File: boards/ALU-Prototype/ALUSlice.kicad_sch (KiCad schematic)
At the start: 12 parts, among them U5 7400, U6 7400, U7 7400, U8 7400

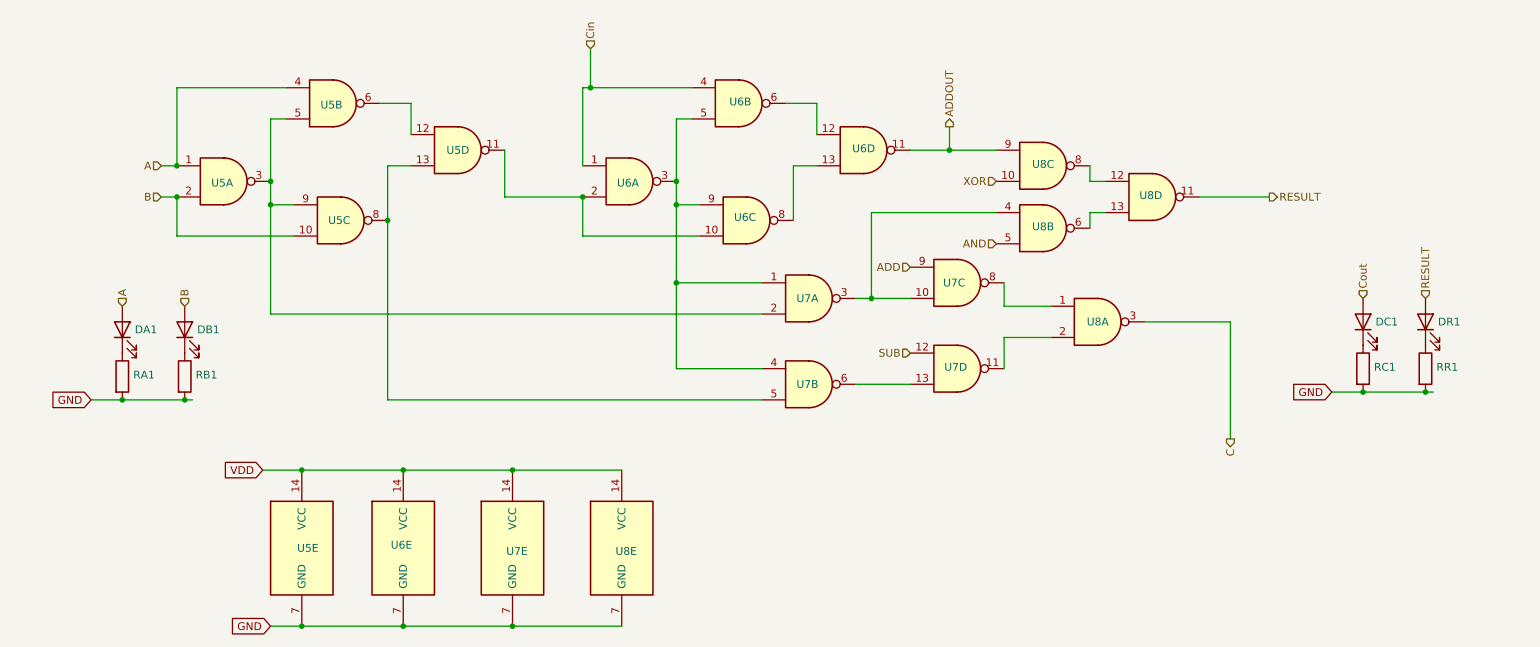
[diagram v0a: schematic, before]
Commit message: pin headers (2*17 and 2*8)
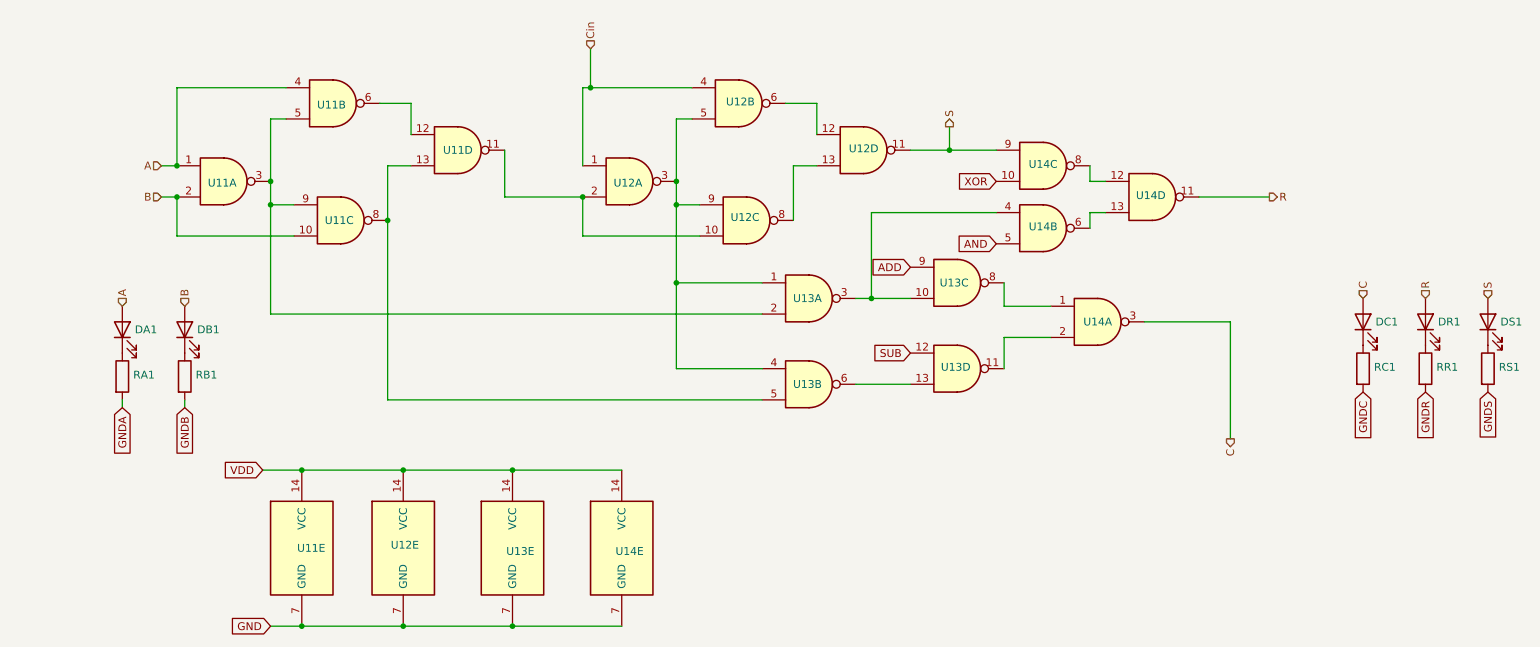
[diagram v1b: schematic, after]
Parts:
- added DS1: LED, LED_SMD:LED_0201_0603Metric, symbol Device:LED
- added RS1: R, Resistor_SMD:R_0201_0603Metric, symbol Device:R
- renumbered U5 to U11, U6 to U12, U7 to U13, U8 to U14
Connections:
- net Cout is gone; now on net C: DC1.2 (A)
- net GND: no longer RA1.2, RB1.2, RC1.2, RR1.2
- net ADDOUT renamed S
- net S: now also DS1.2 (A)
- net RESULT renamed R
- new net: DS1.1 (K), RS1.1
- new net GNDA: RA1.2
- new net GNDB: RB1.2
- new net GNDC: RC1.2
- new net GNDR: RR1.2
- new net GNDS: RS1.2

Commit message: Routing complete. Corrected some errors
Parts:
- DA1, DB1, DC1, DR1, DS1: value LED -> ~; footprint LED_SMD:LED_0201_0603Metric -> LED_SMD:LED_0402_1005Metric; LCSC (none) -> C22355736
- RA1, RB1, RC1, RR1, RS1: value R -> 330; footprint Resistor_SMD:R_0201_0603Metric -> Resistor_SMD:R_0402_1005Metric
- U11, U12, U13, U14: value 7400 -> ~; LCSC (none) -> C5587

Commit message: First try of complete files to JLPCB
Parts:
- RA1, RB1, RC1, RR1, RS1: LCSC (none) -> C12246
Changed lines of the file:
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@@
+			)
+		)
+		(property "LCSC" "C12246"
+			(at 246.38 111.76 0)
+			(effects
+				(font
+					(size 1.27 1.27)
+				)
+				(hide yes)
 			)
 		)
@@
 			)
 		)
-		(property "LCSC" ""
+		(property "LCSC" "C12246"
 			(at 54.61 113.03 0)
 			(effects
@@
 			)
 		)
-		(property "LCSC" ""
+		(property "LCSC" "C12246"
 			(at 256.54 111.76 0)
 			(effects
@@
 			)
 		)
-		(property "LCSC" ""
+		(property "LCSC" "C12246"
 			(at 266.7 111.76 0)
 			(effects
@@
 			)
 		)
-		(property "LCSC" ""
+		(property "LCSC" "C12246"
 			(at 44.45 113.03 0)
 			(effects

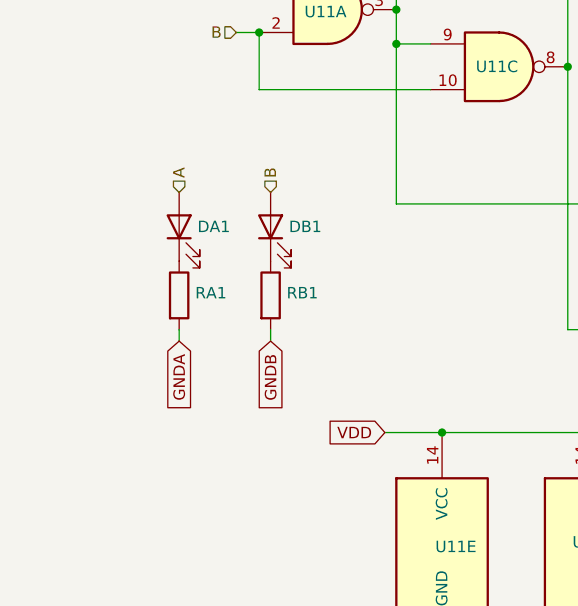
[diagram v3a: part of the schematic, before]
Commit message: Schematic for 8-bit ALU
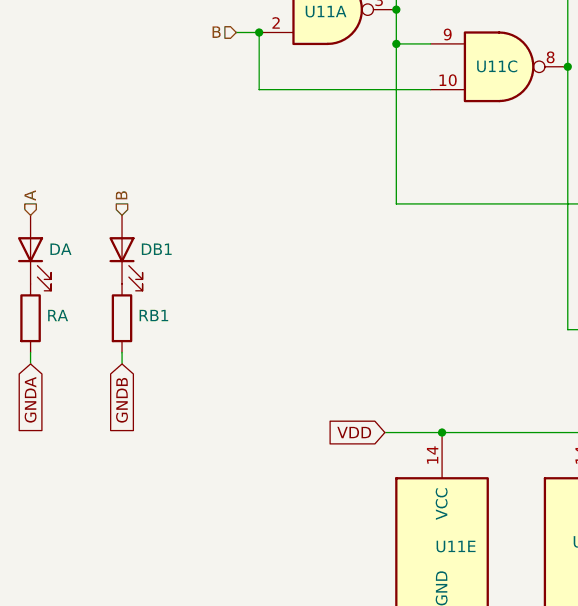
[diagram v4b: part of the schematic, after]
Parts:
- renumbered DA1 to DA, RA1 to RA
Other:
- moved on the sheet: DA, DB1, RA, RB1

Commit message: 8-bit PCB, P1 version
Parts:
- renumbered DA to DA1, RA to RA1

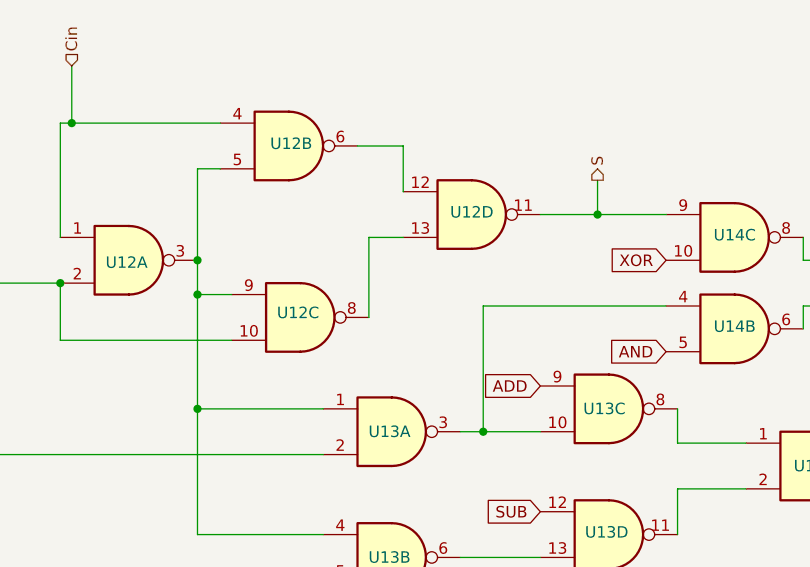
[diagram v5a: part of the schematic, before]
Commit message: Schematic with Equality circuit
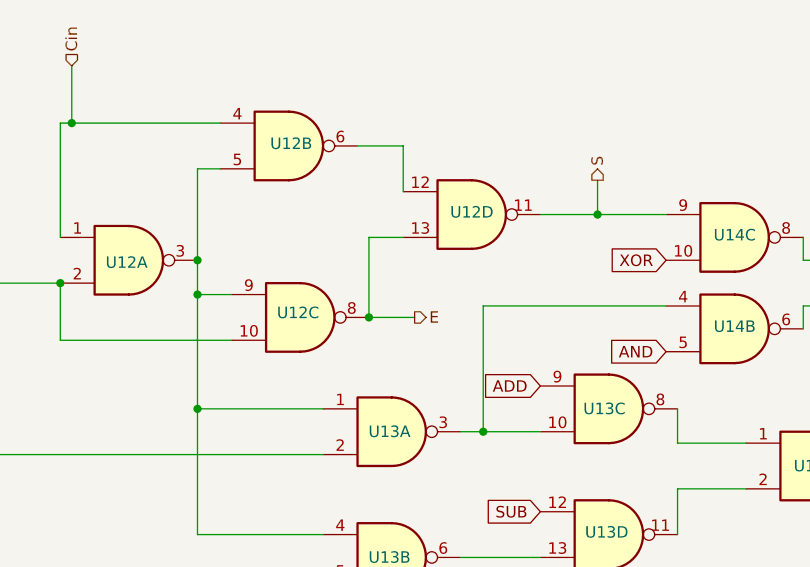
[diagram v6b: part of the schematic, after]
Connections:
- net E: now reaches U12.13, U12.8
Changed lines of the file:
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@@
+	)
+	(junction
+		(at 153.67 87.63)
+		(diameter 0)
+		(color 0 0 0 0)
 	)
 	(junction
@@
 	(wire
 		(pts
+			(xy 158.75 87.63) (xy 153.67 87.63)
+		)
+		(stroke
+			(width 0)
+			(type default)
+		)
+	)
+	(wire
+		(pts
 			(xy 68.58 71.12) (xy 71.12 71.12)
 		)
@@
 	(wire
 		(pts
-			(xy 153.67 87.63) (xy 153.67 78.74)
+			(xy 153.67 78.74) (xy 153.67 87.63)
 		)
 		(stroke
@@
 		)
 	)
+	(hierarchical_label "E"
+		(shape output)
+		(at 158.75 87.63 0)
+		(effects
+			(font
+				(size 1.27 1.27)
+			)
+			(justify left)
+		)
+	)
